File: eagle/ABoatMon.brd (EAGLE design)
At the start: 78.7 x 61 mm, 29 parts, among them J1 VUSB, J2 GND, J3 GND, X1 MKDSN1,5/2-5,08

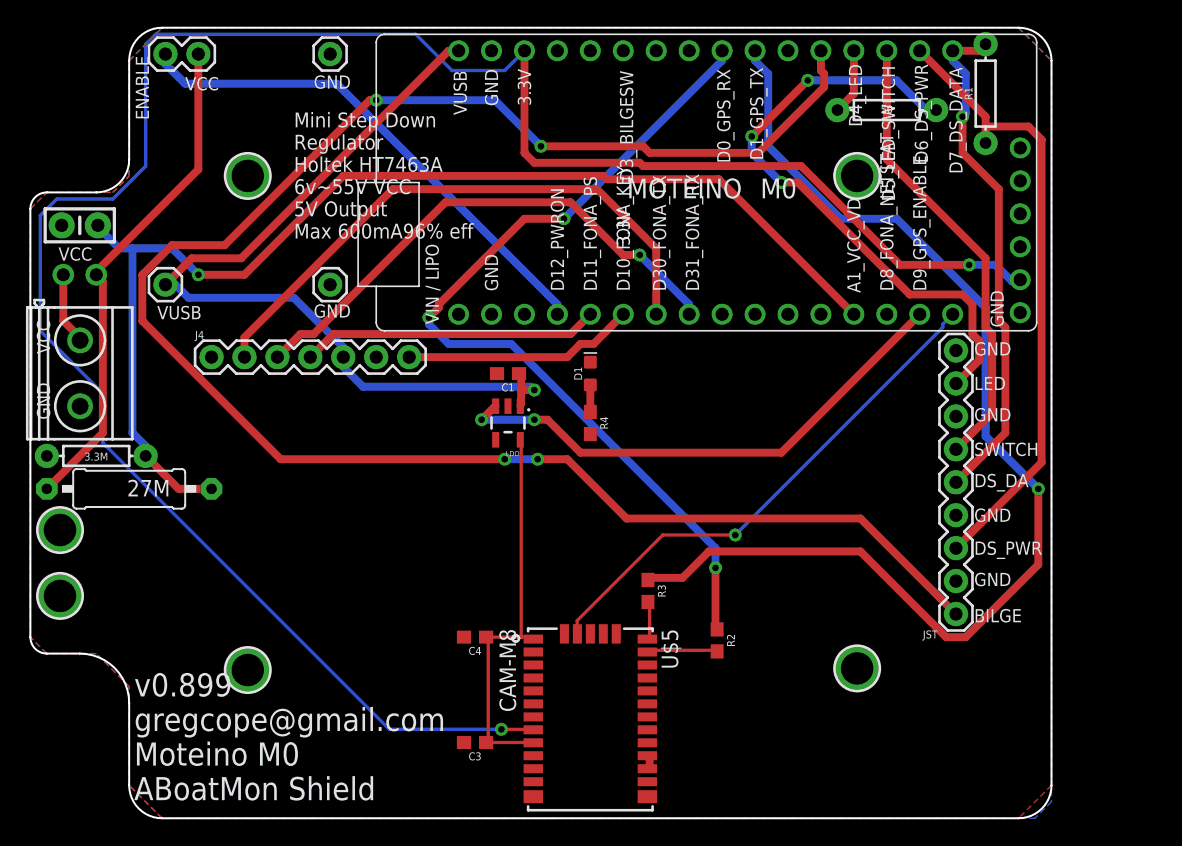
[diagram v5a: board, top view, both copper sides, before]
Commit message: first pass with vias - one airwire
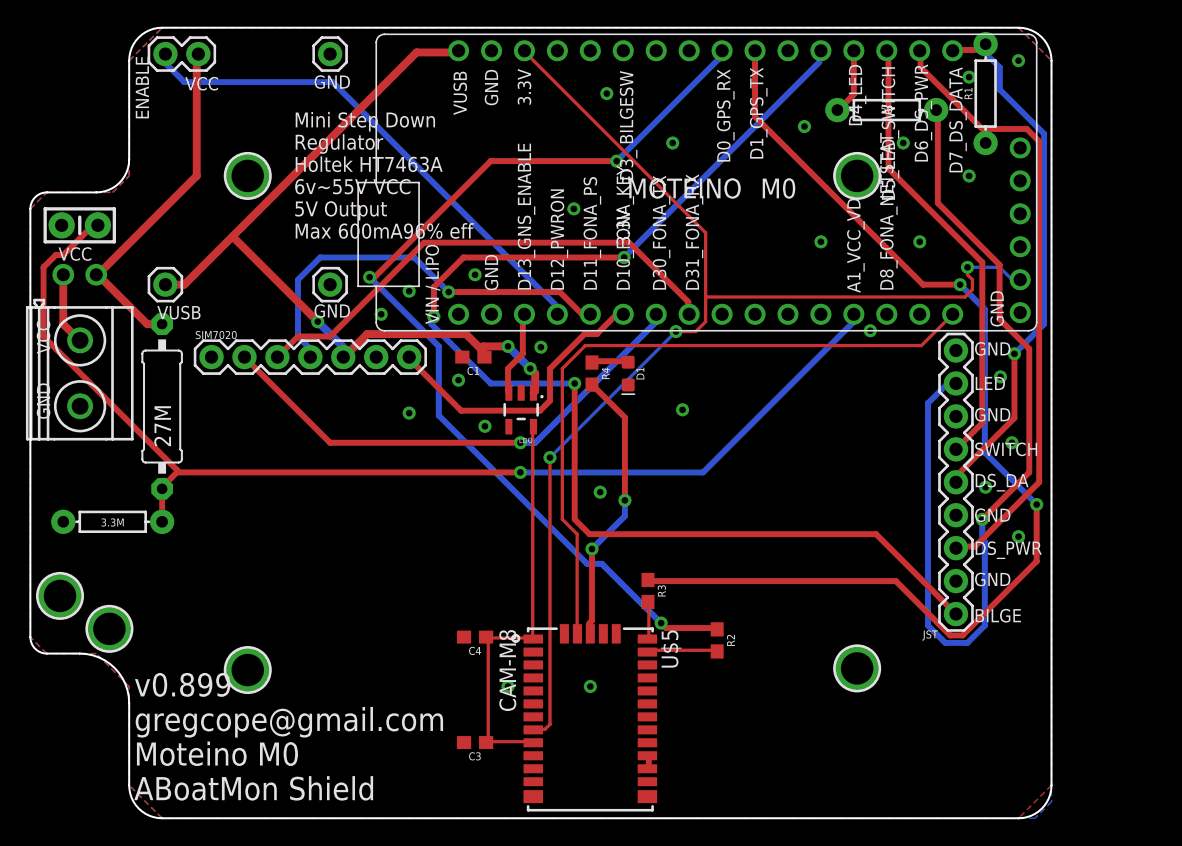
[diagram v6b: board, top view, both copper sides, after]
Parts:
- SIM7020: value (none) -> SIMCOM
- VCC: value (none) -> JUMPER
- moved U$2 8.52 mm to (7.37, 14.6)
- moved R6 6.84 mm to (11.4, 31.8), turned to 90 degrees
- moved R5 5.24 mm to (7.62, 22.9)
- moved R4 3.81 mm to (44.6, 34.3)
- moved C1 2.95 mm to (35.4, 35.6)
- moved D1 2.92 mm to (47.4, 34.3), turned to 270 degrees
- moved LDO 1.44 mm to (39.1, 31.5)
- renumbered J4 to SIM7020
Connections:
- removed net D9_GNS_ENABLE: LDO.3, U$6.D9
- new net D13_GNS_ENABLE: LDO.3, U$6.D13
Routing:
- net 3.3V: track 162.5 -> 92.2 mm, vias 2 -> 3
- net D3_BILGESW: track 140.5 -> 96.6 mm, vias 4 -> 3
- net D9_GNS_ENABLE: track 40.8 -> 0.00 mm, vias 2 -> 0
- net LED: track 47.1 -> 69.7 mm, vias 3 -> 1
- net N$1: track 0.00 -> 21.4 mm, vias 0 -> 2
- net D8_LNA_EN: track 39.9 -> 52.8 mm, vias 1 -> 0
- net VCC_JUMPER: track 38.8 -> 27.0 mm
- net D11_7020_PWRKEY: track 23.0 -> 31.4 mm, vias 0 -> 1
- net D0_RX_GNS: track 67.8 -> 75.8 mm
- net D13_GNS_ENABLE: track 0.00 -> 6.68 mm
- net D30_TX_7020: track 45.0 -> 38.9 mm, vias 0 -> 1
- net D10_7020_SLEEP: track 17.9 -> 22.8 mm
- net VUSB: track 66.5 -> 62.2 mm, vias 1 -> 3
- net D1_TX_GNS: track 87.3 -> 84.2 mm, vias 1 -> 2
- net A1_VCC_VD: track 90.3 -> 87.5 mm
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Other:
- board text added: "D13_GNS_ENABLE"
- board text removed: "D9_GPS_ENABLE"

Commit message: added tab
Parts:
- added J4: LIPO, SparkFun-Connectors:1X01
- moved JST 11.4 mm to (82.8, 20.8)
- moved R5 9.92 mm to (15.2, 29.2), turned to 270 degrees
- moved C1 3.81 mm to (35.4, 31.8)
- moved R1 3.81 mm to (74.9, 52.1)
- moved R4 2.54 mm to (44.5, 31.8)
- moved D1 2.54 mm to (47.4, 31.8)
- moved LDO 2.54 mm to (39.1, 29.0)
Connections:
- new net LIPO: C1.1, J4.1, LDO.1, SIM7020.5
- net 3.3V: no longer U$6.3V3, U$6.3V3_2
- net VUSB: no longer C1.1, LDO.1, SIM7020.5
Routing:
- net 3.3V: track 92.2 -> 0.00 mm, vias 3 -> 0
- net D3_BILGESW: track 96.6 -> 48.3 mm, vias 3 -> 0
- net LIPO: track 0.00 -> 47.4 mm, vias 0 -> 2
- net LED: track 69.7 -> 24.1 mm, vias 1 -> 0
- net VUSB: track 62.2 -> 30.2 mm, vias 3 -> 0
- net D1_TX_GNS: track 84.2 -> 64.4 mm, vias 2 -> 1
- net D0_RX_GNS: track 75.8 -> 61.9 mm, vias 3 -> 0
- net D6_DS_PWR: track 48.7 -> 39.3 mm
- net D8_LNA_EN: track 52.8 -> 44.0 mm
- net D7_DS_DATA: track 41.4 -> 33.7 mm, vias 1 -> 0
- net D13_GNS_ENABLE: track 6.68 -> 12.4 mm
- net A1_VCC_VD: track 87.5 -> 93.2 mm, vias 1 -> 0
- net D12_VCC_PWRON: track 39.3 -> 44.1 mm
- net N$1: track 21.4 -> 16.7 mm, vias 2 -> 0
- net D31_RX_7020: track 38.3 -> 35.0 mm
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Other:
- board size 78.7 x 61 mm -> 85.1 x 61 mm

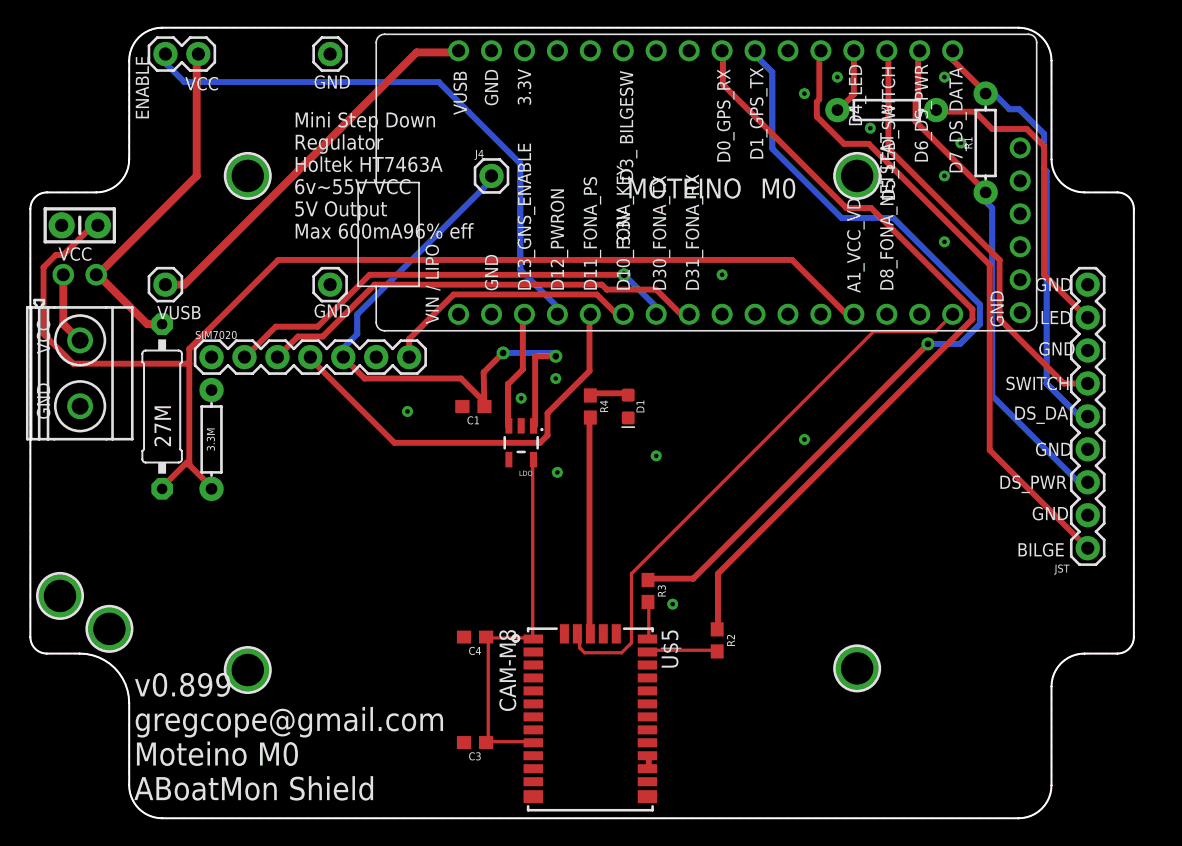
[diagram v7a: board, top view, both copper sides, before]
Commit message: added u.ft, moved GNS
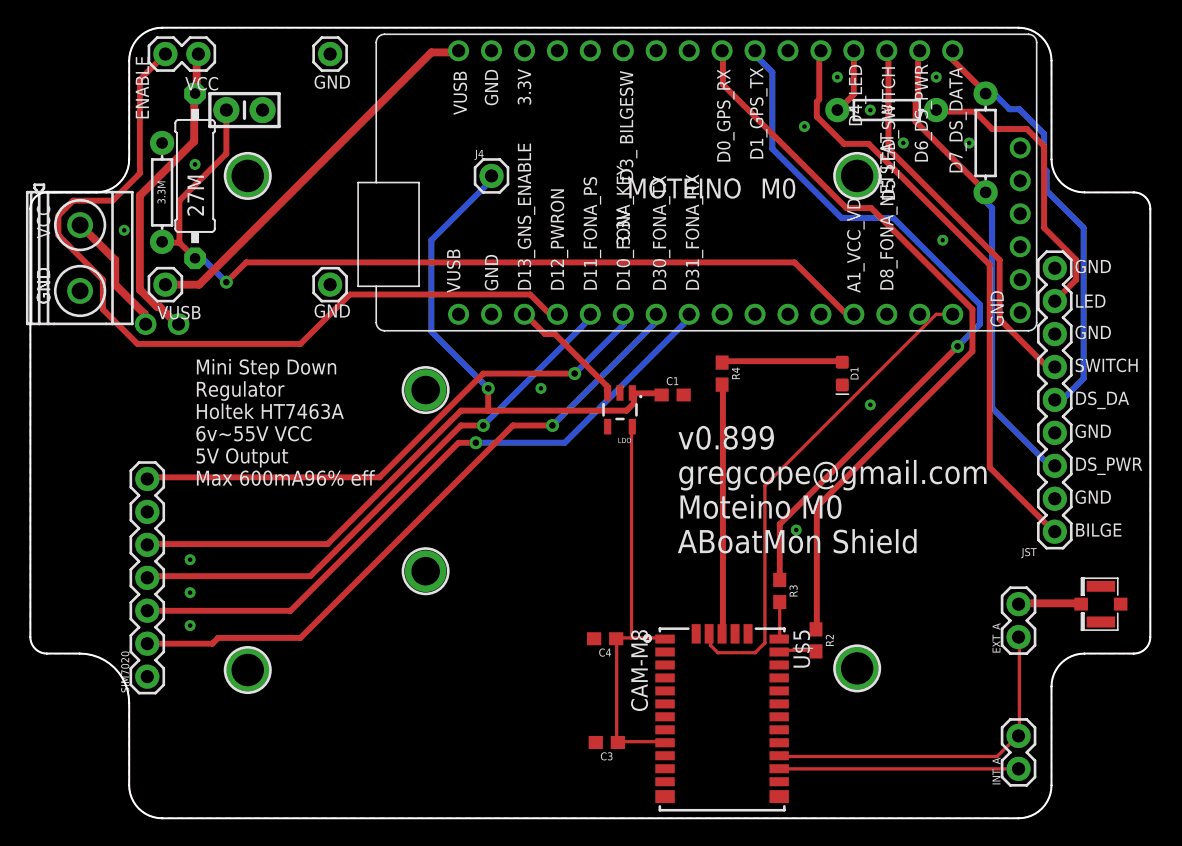
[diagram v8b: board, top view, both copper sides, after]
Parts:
- removed U$2, U$4: MOUNTINGHOLE2.5, microbuilder:MOUNTINGHOLE_2.5_PLATED
- added EXT_A, INT_A: (no value), SparkFun-Connectors:1X02
- added J5: U.FL, SparkFun-Connectors:U.FL
- added U$3, U$9: MOUNTINGHOLE2.0, microbuilder:MOUNTINGHOLE_2.0_PLATED
- moved SIM7020 25.1 mm to (10.3, 10.9), turned to 90 degrees
- moved R5 19.4 mm to (11.4, 48.3)
- moved R6 18.0 mm to (14.0, 49.5)
- moved D1 16.7 mm to (63.9, 34.3)
- moved C2 15.5 mm to (17.8, 54.6), turned to 0 degrees
- moved C1 15.4 mm to (50.8, 32.6), turned to 0 degrees
- moved R4 10.5 mm to (54.6, 34.3)
- moved C3 10.2 mm to (45.7, 5.84)
- moved R3 10.2 mm to (59.1, 17.5)
- moved U$5 10.2 mm to (54.6, 7.62)
- moved C4 10.0 mm to (45.6, 13.8)
- moved X1 8.89 mm to (5.08, 43.2)
- moved LDO 8.03 mm to (46.7, 31.5)
- moved R2 7.62 mm to (61.8, 13.7)
- moved VCC 7.41 mm to (11.4, 38.1)
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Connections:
- new net N$6: EXT_A.2, J5.FEED
- new net N$7: INT_A.1, U$5.16
- net GND: now also J5.1, J5.2
- net N$5: now also EXT_A.1, INT_A.2; no longer U$5.16
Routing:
- net N$5: track 1.10 -> 26.8 mm
- net A1_VCC_VD: track 93.2 -> 68.7 mm, vias 0 -> 1
- net D10_7020_SLEEP: track 20.0 -> 42.6 mm, vias 0 -> 1
- net D12_VCC_PWRON: track 44.1 -> 64.7 mm
- net LIPO: track 47.4 -> 67.1 mm, vias 2 -> 1
- net N$7: track 0.00 -> 18.5 mm
- net D31_RX_7020: track 35.0 -> 51.5 mm, vias 0 -> 1
- net D30_TX_7020: track 36.0 -> 50.1 mm
- net D11_7020_PWRKEY: track 32.1 -> 42.9 mm, vias 0 -> 1
- net D1_TX_GNS: track 64.4 -> 56.7 mm
- net N$4: track 3.06 -> 9.36 mm
- net D8_LNA_EN: track 44.0 -> 37.7 mm
- net N$6: track 0.00 -> 4.86 mm
- net VCC: track 5.61 -> 9.78 mm
- net D13_GNS_ENABLE: track 12.4 -> 9.19 mm
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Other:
- board size 85.1 x 61 mm -> 86.4 x 61 mm
- board text removed: "VIN / LIPO"
